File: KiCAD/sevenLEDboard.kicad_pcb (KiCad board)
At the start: 2 copper layers, 23.1 x 20 mm, 14 parts, among them J1 Conn_01x03_Male, U1 SC4541

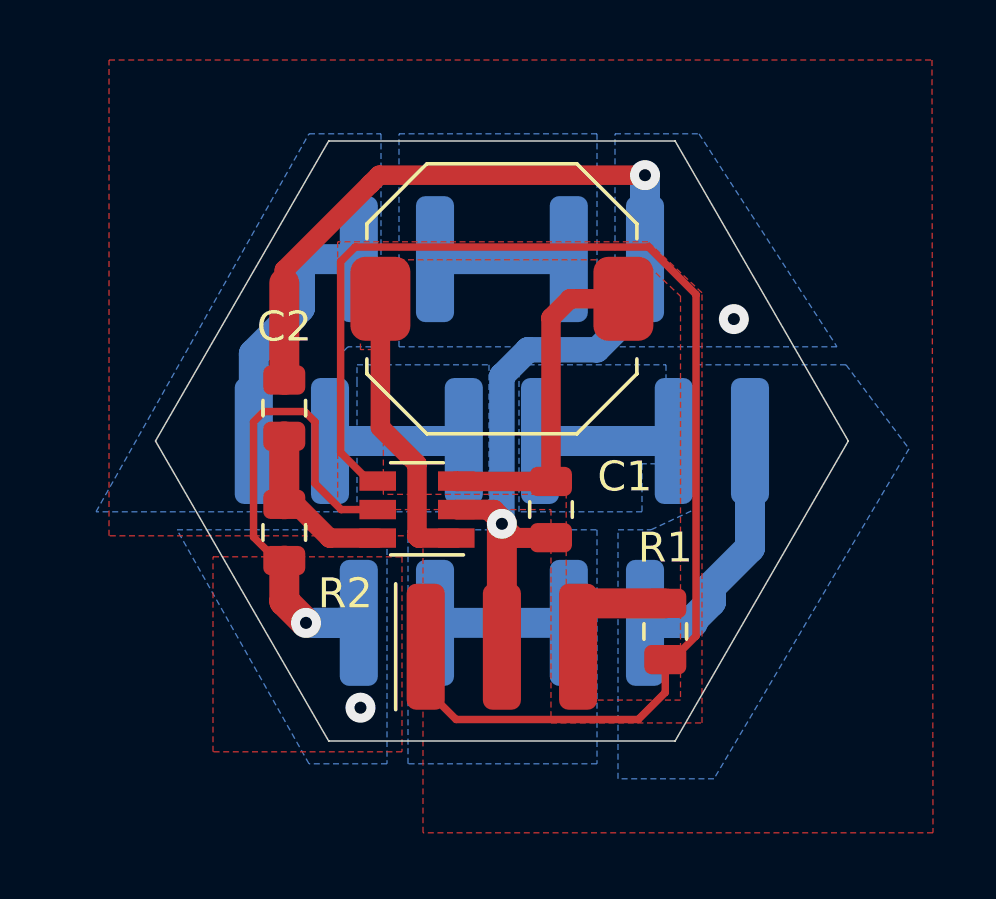
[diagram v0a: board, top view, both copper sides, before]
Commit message: Created production 7 LED board with ZXLD1350 DC-DC bucking regulator.
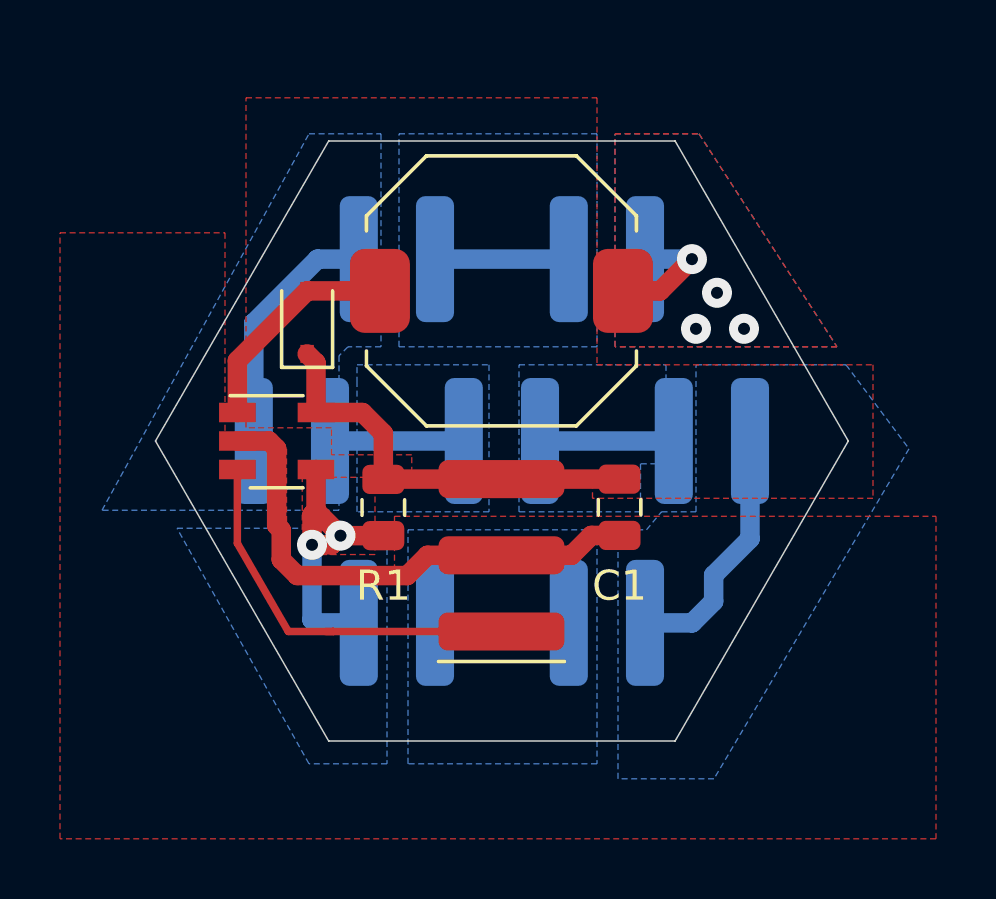
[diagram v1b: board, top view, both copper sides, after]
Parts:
- removed C2: 10uF, Capacitor_SMD:C_0805_2012Metric
- removed R2: 2, Resistor_SMD:R_0805_2012Metric
- added D8: D_Schottky, Diode_SMD:D_SOD-323, F.Cu at (138.9, 74.8)
- R1: value 10k -> 1
- U1: value SC4541 -> ZXLD1350; footprint Package_TO_SOT_SMD:TSOT-23-6 -> Package_TO_SOT_SMD:TSOT-23-5
- moved R1 10.3 mm to (141.5, 81.0)
- moved U1 5.21 mm to (137.9, 78.7), turned to 0 degrees
- moved J1 2.58 mm to (145.4, 85.1), turned to 90 degrees
- moved C1 2.29 mm to (149.4, 80.9)
- moved L1 0.26 mm to (145.4, 73.7)
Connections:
- D7 pad 1: GND -> Net-(D7-Pad1)
- L1 pad 1: VS -> Net-(D7-Pad1)
- R1 pad 1: Net-(J1-Pad1) -> Net-(D1-Pad2)
- U1 pad 3: VS -> Net-(J1-Pad1)
- U1 pad 4: Net-(J1-Pad1) -> Net-(D1-Pad2)
- U1 pad 5: Net-(D1-Pad2) -> VS
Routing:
- net Net-(J1-Pad1): track 45.0 -> 13.2 mm
- net GND: track 43.0 -> 17.2 mm, vias 3 -> 0
- net Net-(D1-Pad2): track 17.0 -> 10.3 mm
- net Net-(C2-Pad1): track 5.46 -> 0.00 mm
- net Net-(D7-Pad1): track 0.00 -> 4.30 mm, vias 0 -> 4
- net VS: track 17.2 -> 14.0 mm
- net Net-(D8-Pad2): track 9.76 -> 7.44 mm
- net Net-(D2-Pad1): track 9.99 -> 8.43 mm
- added copper zone on B.Cu, net Net-(D7-Pad1)
- added copper zone on F.Cu, net Net-(D7-Pad1)
- removed copper zone on B.Cu, net GND
